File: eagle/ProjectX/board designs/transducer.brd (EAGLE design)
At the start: 100 x 80 mm, 20 parts

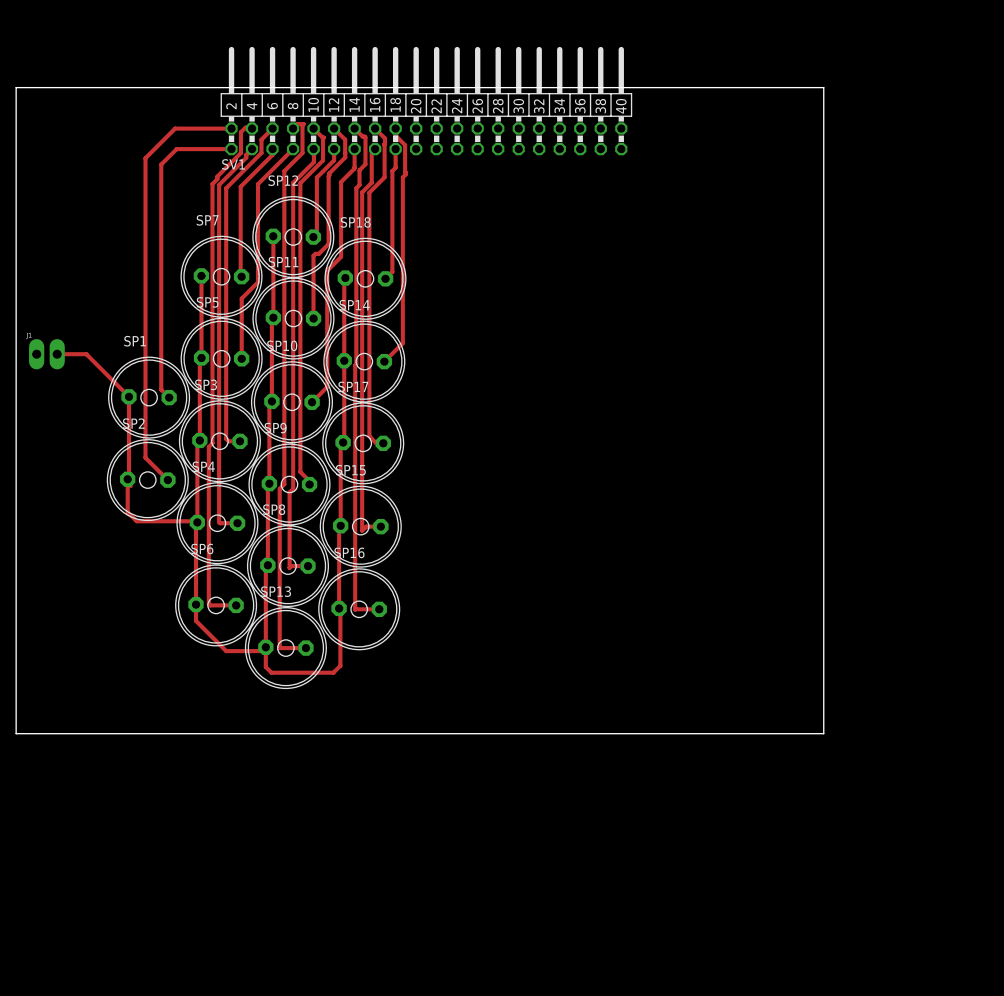
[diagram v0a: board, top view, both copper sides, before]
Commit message: Some work on a transducer board
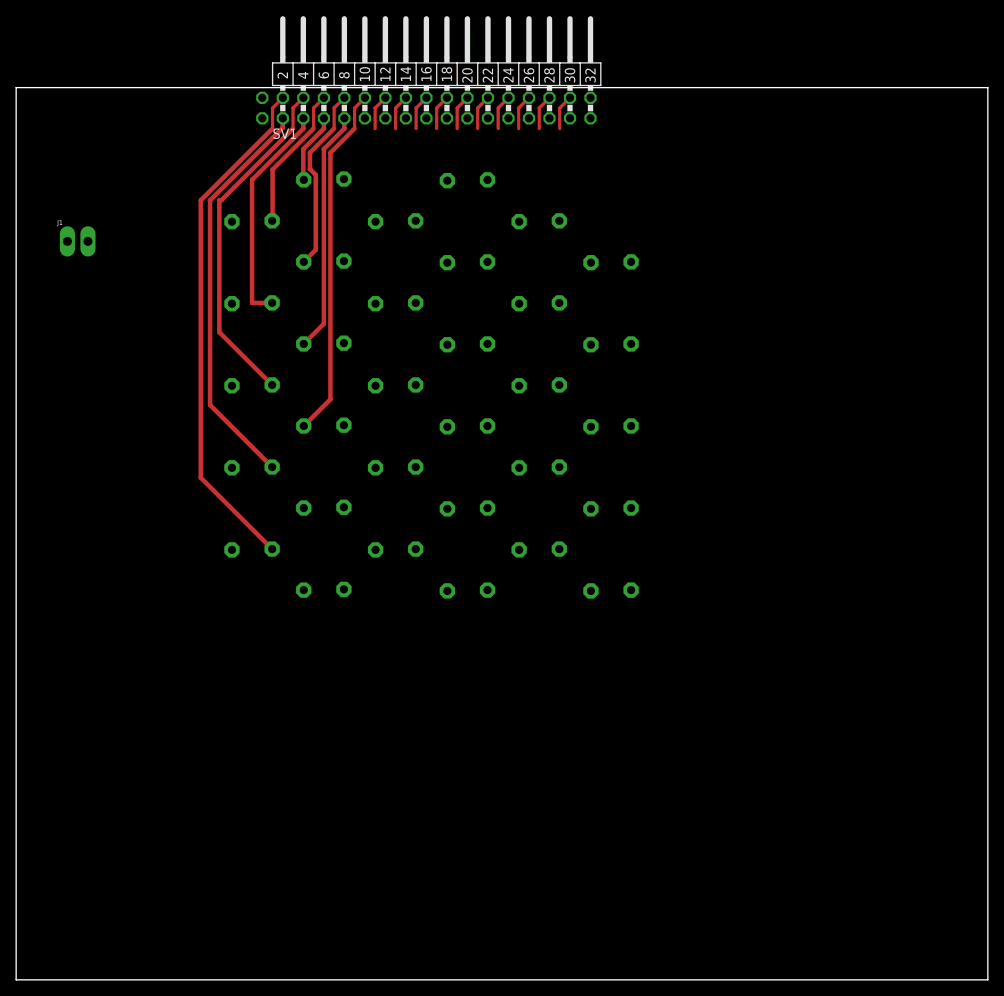
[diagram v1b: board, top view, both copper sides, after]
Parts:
- added SP19, SP20, SP21, SP22, SP23, SP24, SP25, SP30, SP31, SP32, SP33, SP34, SP35, SP36: MA40S4S, transducerlibrary:MA40
- SV1: device con-lstb:MA20-2W -> Parts:MA20-2W
- moved SP13 48.0 mm to (38.1, 58.4), flipped to the bottom
- moved SP12 40.7 mm to (47.0, 22.9), flipped to the bottom, turned to 180 degrees
- moved SP15 38.1 mm to (47.0, 63.5), flipped to the bottom, turned to 180 degrees
- moved SP11 33.8 mm to (38.1, 17.8), flipped to the bottom
- moved SP18 31.1 mm to (55.9, 27.9), flipped to the bottom, turned to 180 degrees
- moved SP14 31.0 mm to (55.9, 17.8), flipped to the bottom, turned to 180 degrees
- moved SP6 27.7 mm to (29.2, 43.2), flipped to the bottom, turned to 180 degrees
- moved SP4 27.6 mm to (29.2, 53.3), flipped to the bottom, turned to 180 degrees
- moved SP3 27.6 mm to (29.2, 63.5), flipped to the bottom, turned to 180 degrees
- moved SP16 18.2 mm to (47.0, 33.0), flipped to the bottom, turned to 180 degrees
- moved SP17 17.8 mm to (47.0, 53.3), flipped to the bottom, turned to 180 degrees
- moved SP7 17.4 mm to (38.1, 68.6), flipped to the bottom
- moved SP2 15.5 mm to (29.2, 22.9), flipped to the bottom, turned to 180 degrees
- moved SP1 15.4 mm to (29.2, 33.0), flipped to the bottom, turned to 180 degrees
- moved J1 14.5 mm to (6.35, 61.0)
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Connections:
- removed net N$21: J1.2, SP1.-, SP10.-, SP11.-, SP12.-, SP13.-, SP14.-, SP15.-, SP16.-, SP17.-, SP18.-, SP2.-, SP3.-, SP4.-, SP5.-, SP6.-, SP7.-, SP8.-, SP9.-
- new net GND: J1.2, SP1.-, SP10.-, SP11.-, SP12.-, SP13.-, SP14.-, SP15.-, SP16.-, SP17.-, SP18.-, SP19.-, SP2.-, SP20.-, SP21.-, SP22.-, SP23.-, SP24.-, SP25.-, SP3.-, SP30.-, SP31.-, SP32.-, SP33.-, SP34.-, SP35.-, SP36.-, SP4.-, SP5.-, SP6.-, SP7.-, SP8.-, SP9.-, SV1.GND, SV1.GND+1
- new net N$10: SP19.+, SV1.20
- new net N$22: SP20.+, SV1.22
- new net N$23: SP21.+, SV1.24
- new net N$24: SP22.+, SV1.26
- new net N$25: SP23.+, SV1.28
- new net N$26: SP24.+, SV1.30
- new net N$27: SP25.+, SV1.32
- new net N$28: SP30.+, SV1.19
- new net N$29: SP31.+, SV1.21
- new net N$30: SP32.+, SV1.23
- new net N$31: SP33.+, SV1.25
- new net N$32: SP34.+, SV1.27
- new net N$33: SP35.+, SV1.29
- new net N$34: SP36.+, SV1.31
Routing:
- net N$21: track 202.0 -> 0.00 mm
- net N$17: track 63.8 -> 4.34 mm
- net N$11: track 55.5 -> 0.00 mm
- net N$2: track 50.5 -> 0.00 mm
- net N$12: track 70.9 -> 23.0 mm
- net N$18: track 41.6 -> 4.34 mm
- net N$15: track 33.5 -> 0.00 mm
- net N$20: track 30.5 -> 4.34 mm
- net N$9: track 42.6 -> 17.9 mm
- net N$6: track 65.2 -> 42.7 mm
- net N$5: track 50.2 -> 28.0 mm
- net N$16: track 26.0 -> 4.34 mm
- net N$19: track 16.6 -> 0.00 mm
- net N$13: track 12.0 -> 0.00 mm
- net N$1: track 38.8 -> 50.1 mm
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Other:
- board size 100 x 80 mm -> 120.3 x 110.5 mm
